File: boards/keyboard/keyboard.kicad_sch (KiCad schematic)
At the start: 64 parts, among them J1 Keyboard Connector, T1 MountingHole_3.2mm_M3, T2 MountingHole_3.2mm_M3, T3 MountingHole_3.2mm_M3

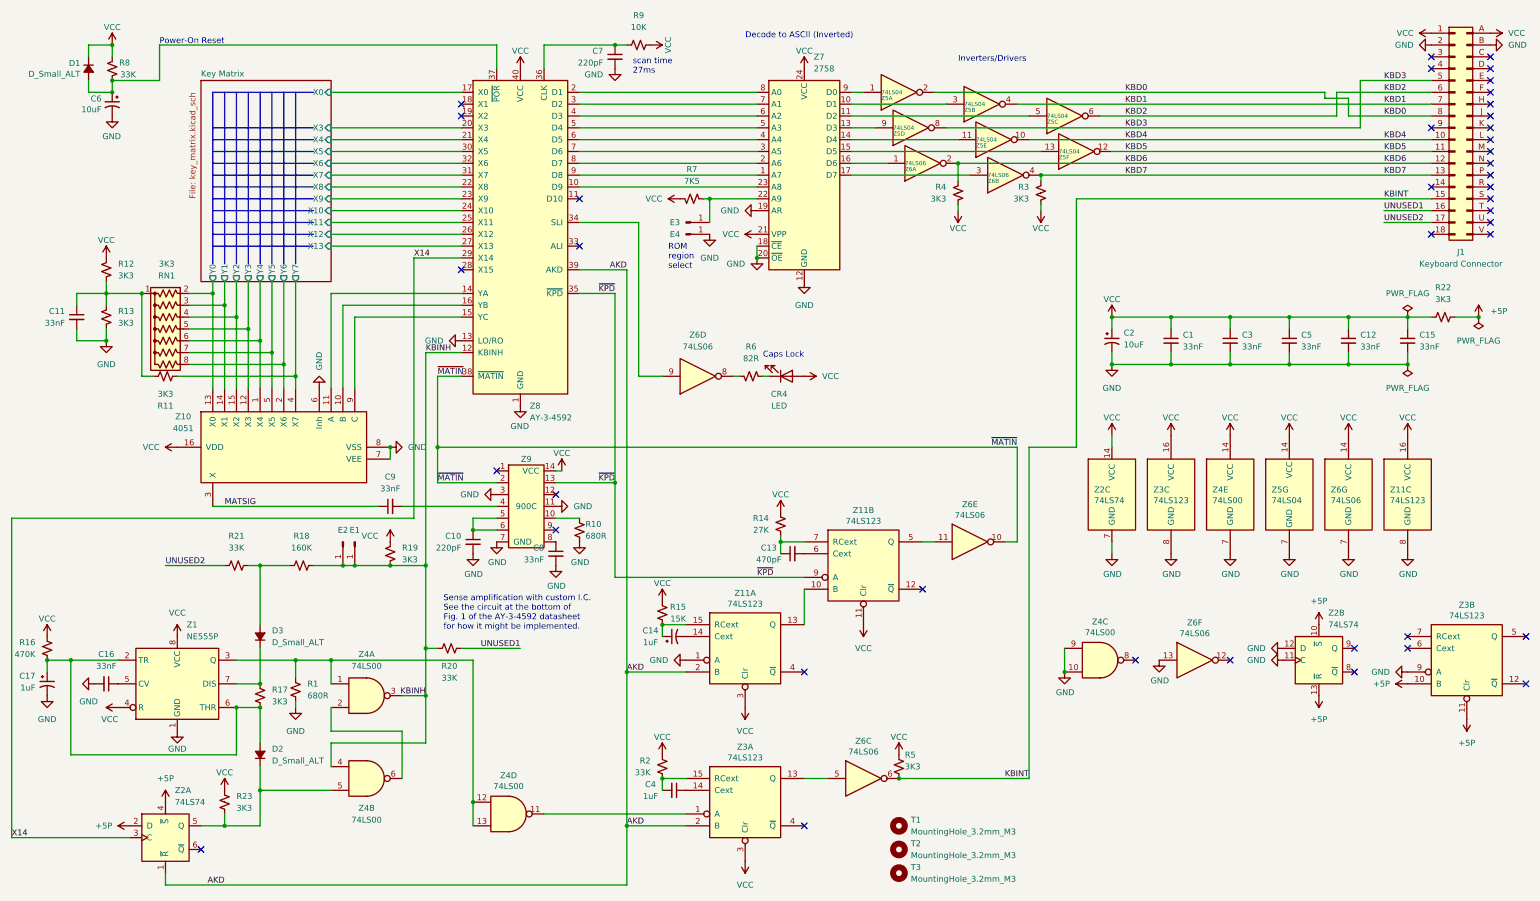
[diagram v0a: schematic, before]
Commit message: Update to KiCad 8
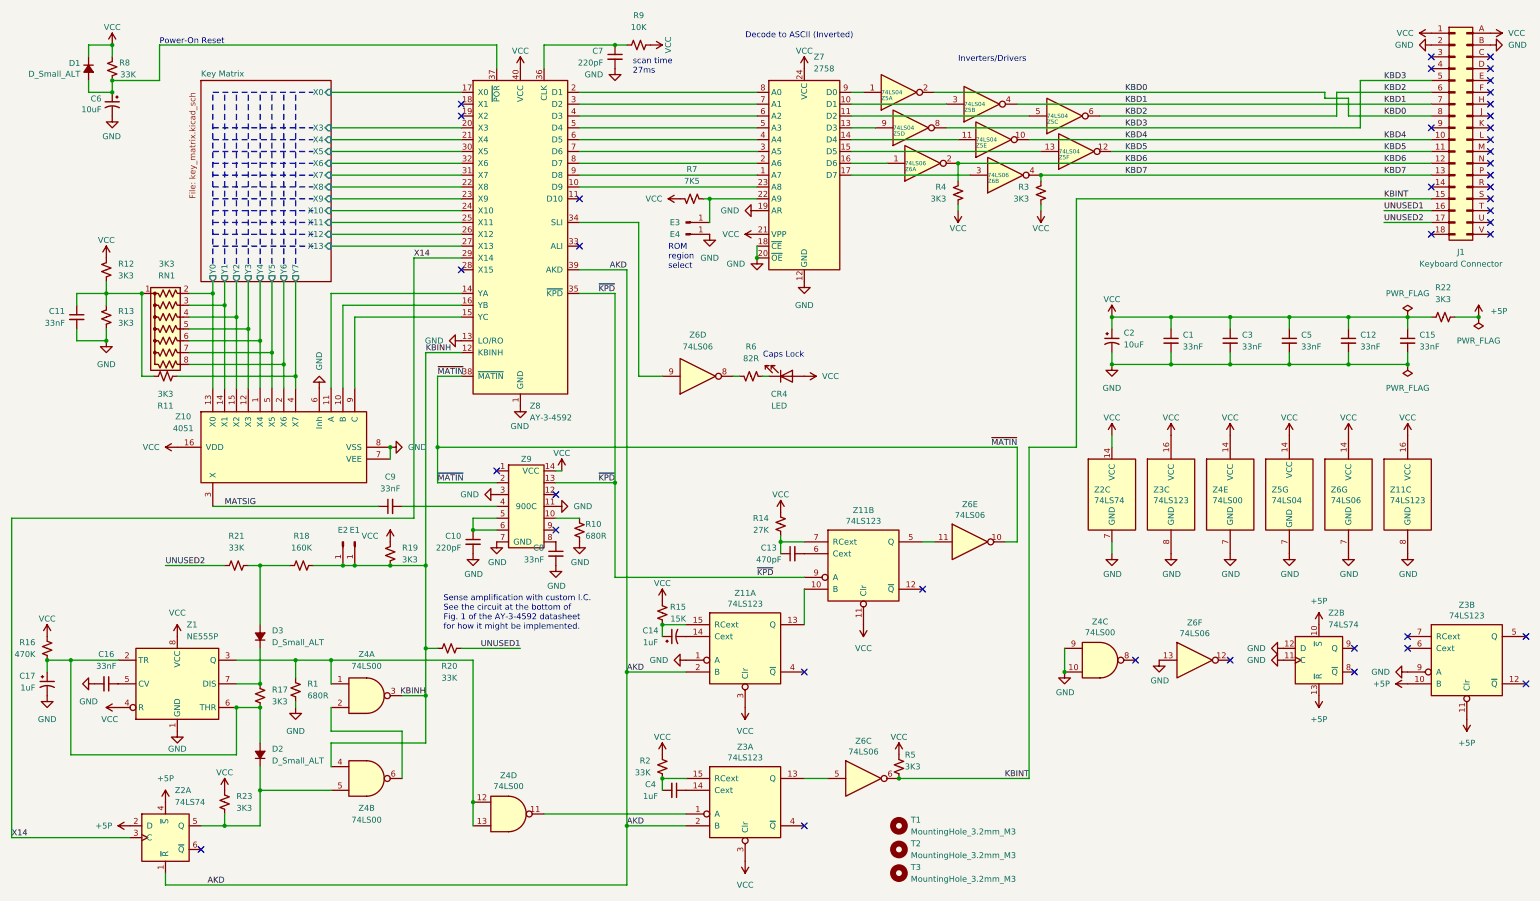
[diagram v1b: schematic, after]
